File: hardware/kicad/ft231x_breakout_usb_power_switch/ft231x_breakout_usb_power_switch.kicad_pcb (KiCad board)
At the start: 2 copper layers, 60 x 31.2 mm, 50 parts, among them J1 USB_B_Micro_ALT, J2 USB_A_ALT, J3 Conn_01x08, J4 Conn_01x06, J5 Conn_01x08, Q3 2N7002, U1 SOT-23-6, U2 FT231XS, U3 SOT-23-6, U4 SOT-23-5

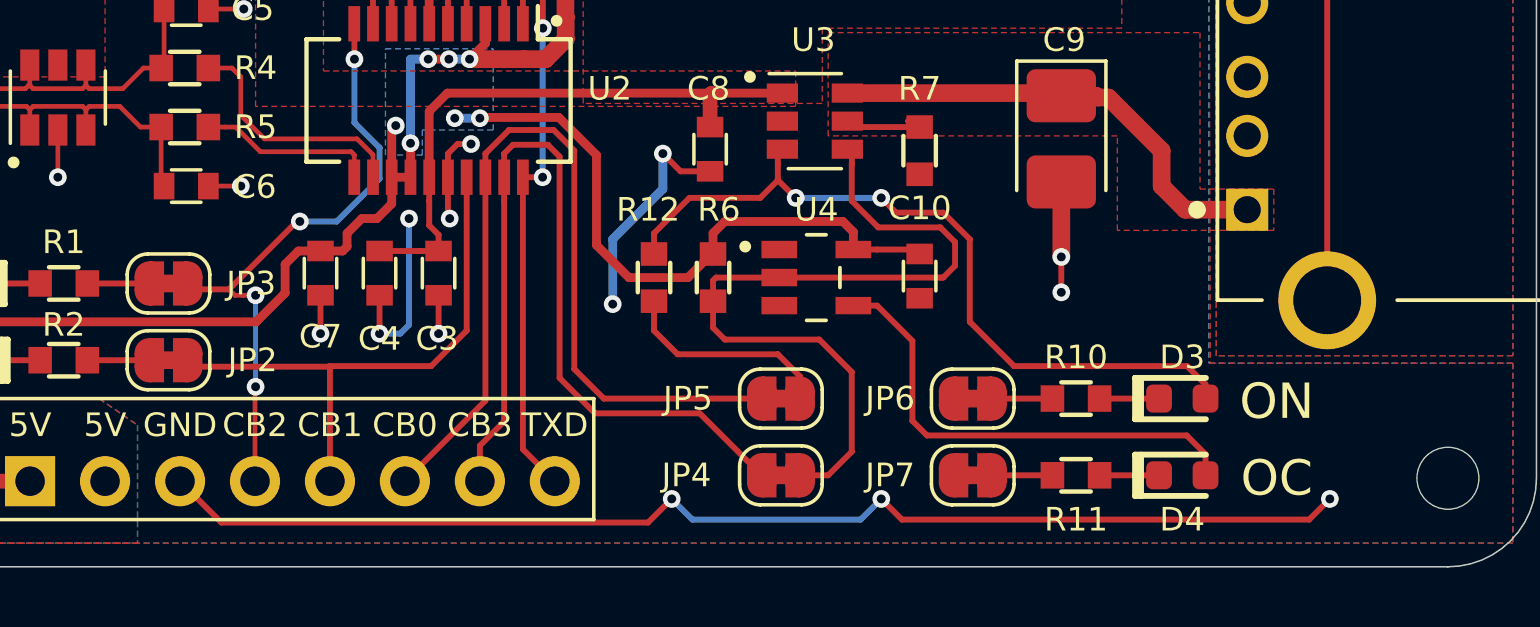
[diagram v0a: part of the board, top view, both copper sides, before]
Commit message: reset switch initial
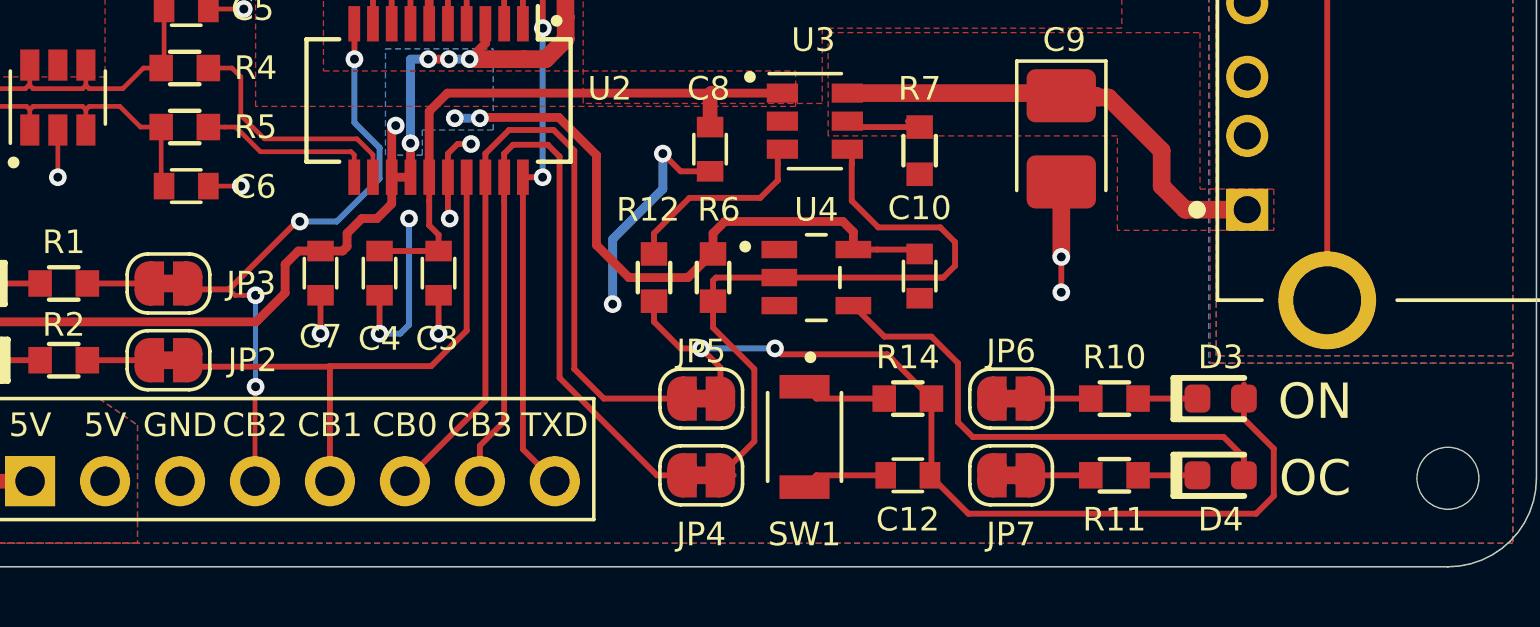
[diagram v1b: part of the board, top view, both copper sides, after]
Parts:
- added C12: 0.1uF, -Passive:C_0603, F.Cu at (148.7, 97.5)
- added R14: 1k, -Passive:R_0603, F.Cu at (148.7, 94.9)
- added SW1: SW_MEC_5G, -Switch:B3U-1000P, F.Cu at (145.2, 96.2)
- U1: value SOT-23-6 -> SRV05-4
- U3: value SOT-23-6 -> TPS2553DBVR
- U4: value SOT-23-5 -> SN74LVC1G04DBVR
- moved JP4 2.70 mm to (141.7, 97.5)
- moved JP5 2.70 mm to (141.7, 94.9)
- moved D3 1.30 mm to (159.3, 94.9)
- moved D4 1.30 mm to (159.3, 97.5)
- moved JP6 1.30 mm to (152.2, 94.9)
- moved JP7 1.30 mm to (152.2, 97.5)
- moved R10 1.30 mm to (155.7, 94.9)
- moved R11 1.30 mm to (155.7, 97.5)
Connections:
- JP5 pad 1: Net-(JP5-Pad1) -> /ENLED
- R12 pad 1: Net-(JP5-Pad1) -> /ENLED
- R12 pad 2: /ENLED -> Net-(R12-Pad2)
- U3 pad 3: /ENLED -> Net-(R12-Pad2)
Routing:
- net GND: track 111.3 -> 73.2 mm, vias 27 -> 24
- net Net-(JP5-Pad1): track 7.44 -> 0.00 mm
- net Net-(R12-Pad2): track 0.00 -> 6.60 mm
- net /ENLED: track 26.1 -> 32.5 mm
- net /FAULT: track 26.7 -> 23.6 mm
- net Net-(R14-Pad1): track 0.00 -> 2.87 mm
- net /GPO: track 30.0 -> 27.3 mm
- net /GPI: track 29.3 -> 26.6 mm
- net Net-(D4-Pad2): track 16.8 -> 17.6 mm

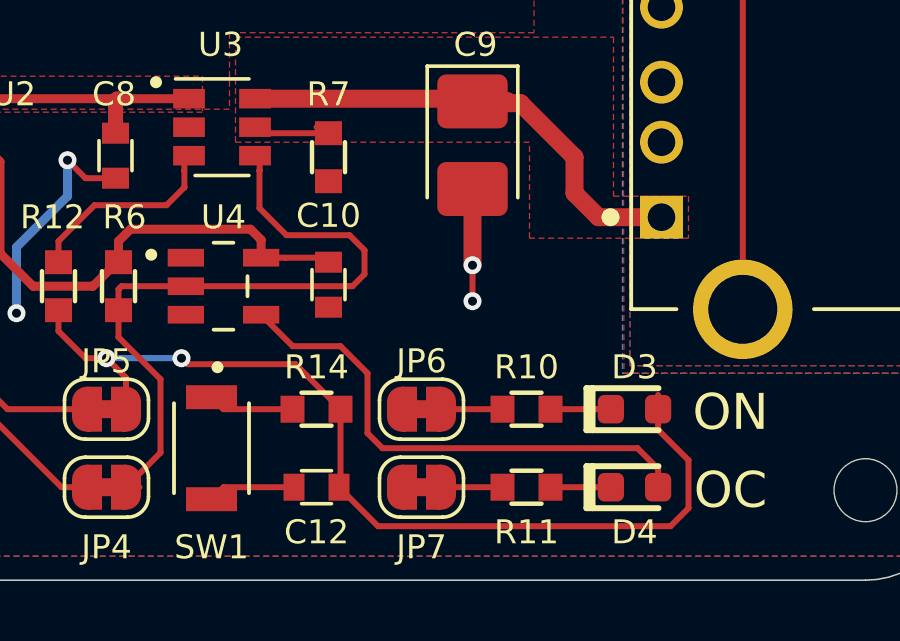
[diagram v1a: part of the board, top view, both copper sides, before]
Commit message: fix unconnected ground
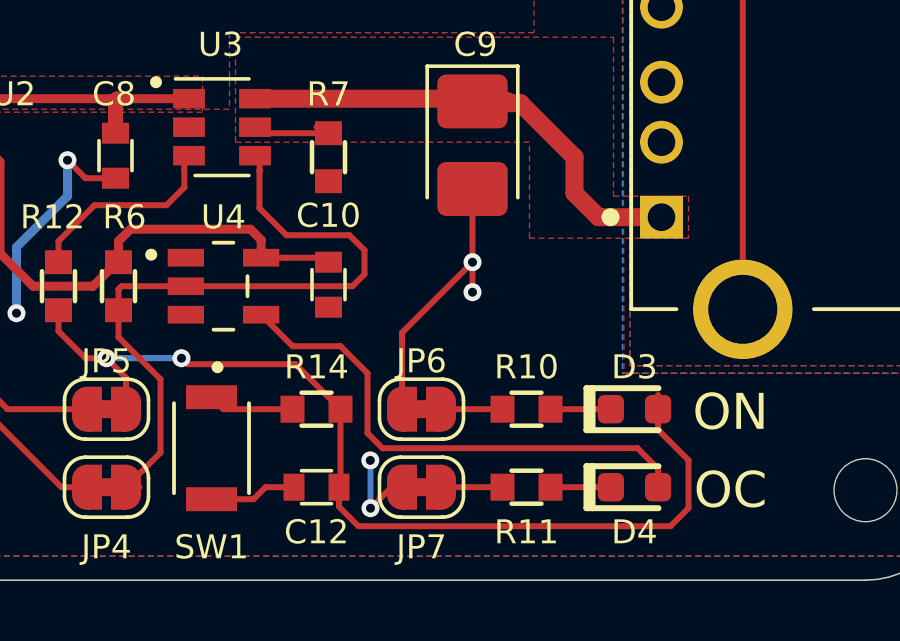
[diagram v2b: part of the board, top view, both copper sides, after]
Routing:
- net GND: track 73.2 -> 81.7 mm, vias 24 -> 26

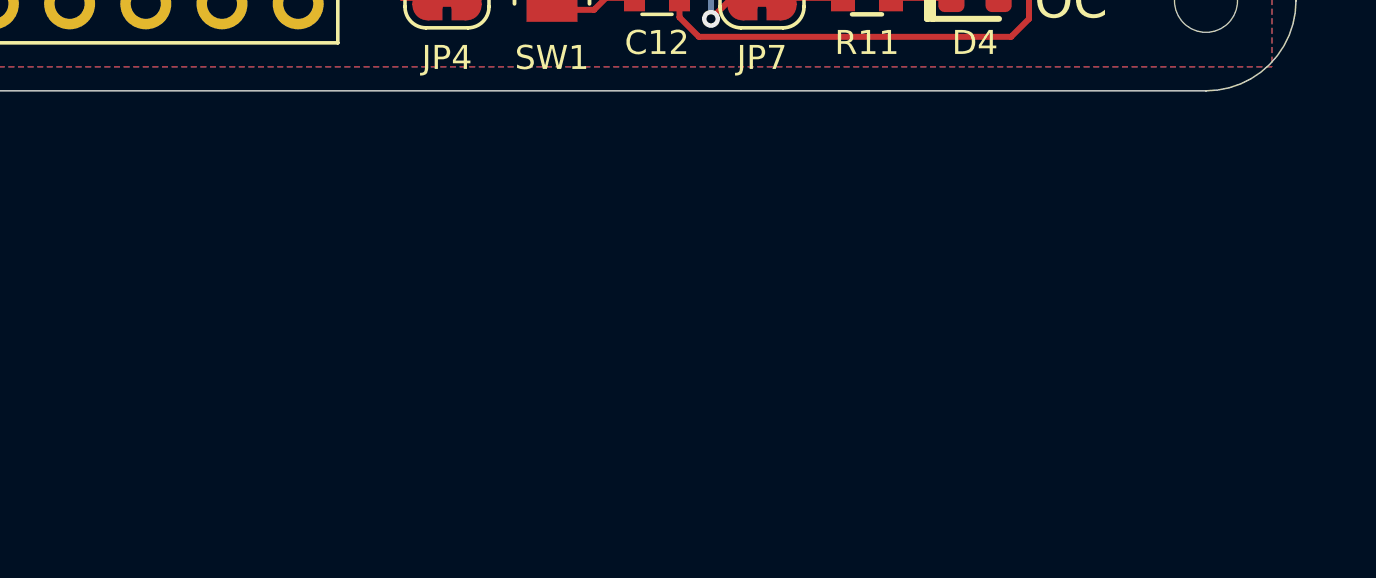
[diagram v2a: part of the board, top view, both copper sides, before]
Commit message: add optional pull down to enable
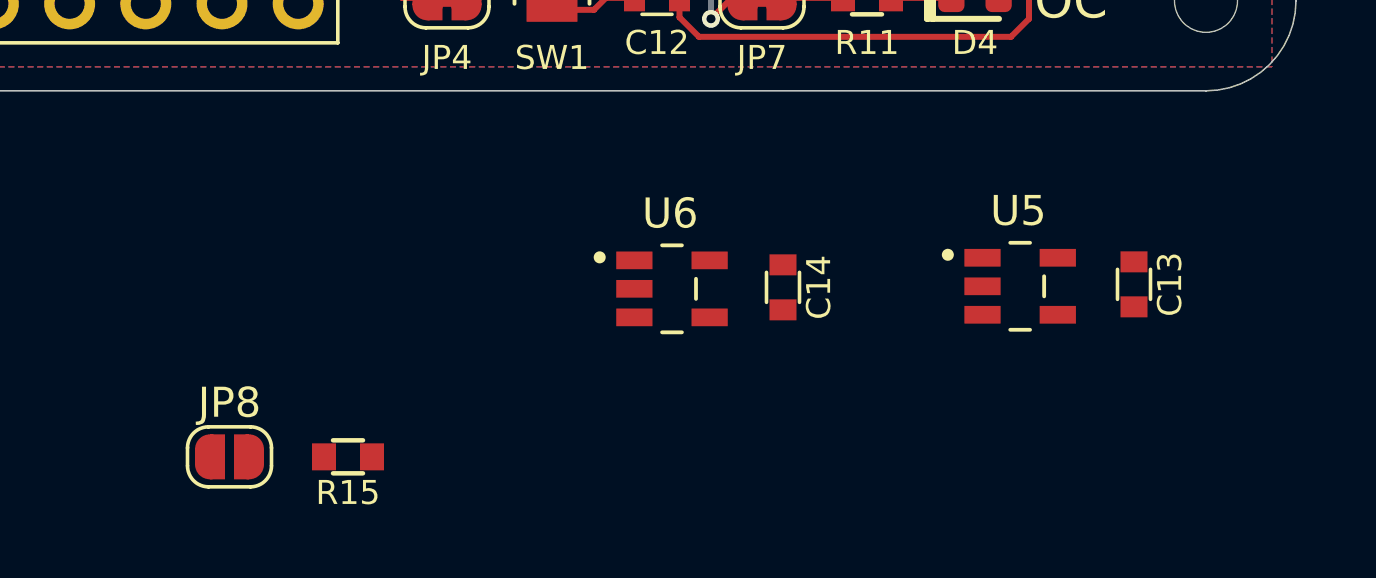
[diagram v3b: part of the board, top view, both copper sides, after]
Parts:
- added C13: 0.1uF, -Passive:C_0603, F.Cu at (164.6, 107.0)
- added C14: 0.1uF, -Passive:C_0603, F.Cu at (152.9, 107.2)
- added JP8: SolderJumper_2_Bridged_Alt, -Jumper:SolderJumper-2_P1.3mm_Un-Bridged_RoundedPad1.0x1.5mm, F.Cu at (134.4, 112.8)
- added R15: 1k, -Passive:R_0603, F.Cu at (138.4, 112.8)
- added U5: NC7SZ66M5X, -Chip:SOT-23-5, F.Cu at (160.8, 107.1)
- added U6: NC7SZ66M5X, -Chip:SOT-23-5, F.Cu at (149.2, 107.2)
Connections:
- net /ENLED renamed /EN
- C8 pad 1: +5V -> GND
- C8 pad 2: GND -> +5V
- J4 pad 4: /TXD -> /STXD
- J4 pad 6: /RESET -> /SRES
- Q3 pad 3: /RESET -> /RES
- R9 pad 1: /RESET -> /RES
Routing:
- net GND: track 81.7 -> 74.1 mm, vias 26 -> 24
- net +5V: track 21.8 -> 29.5 mm, vias 0 -> 2

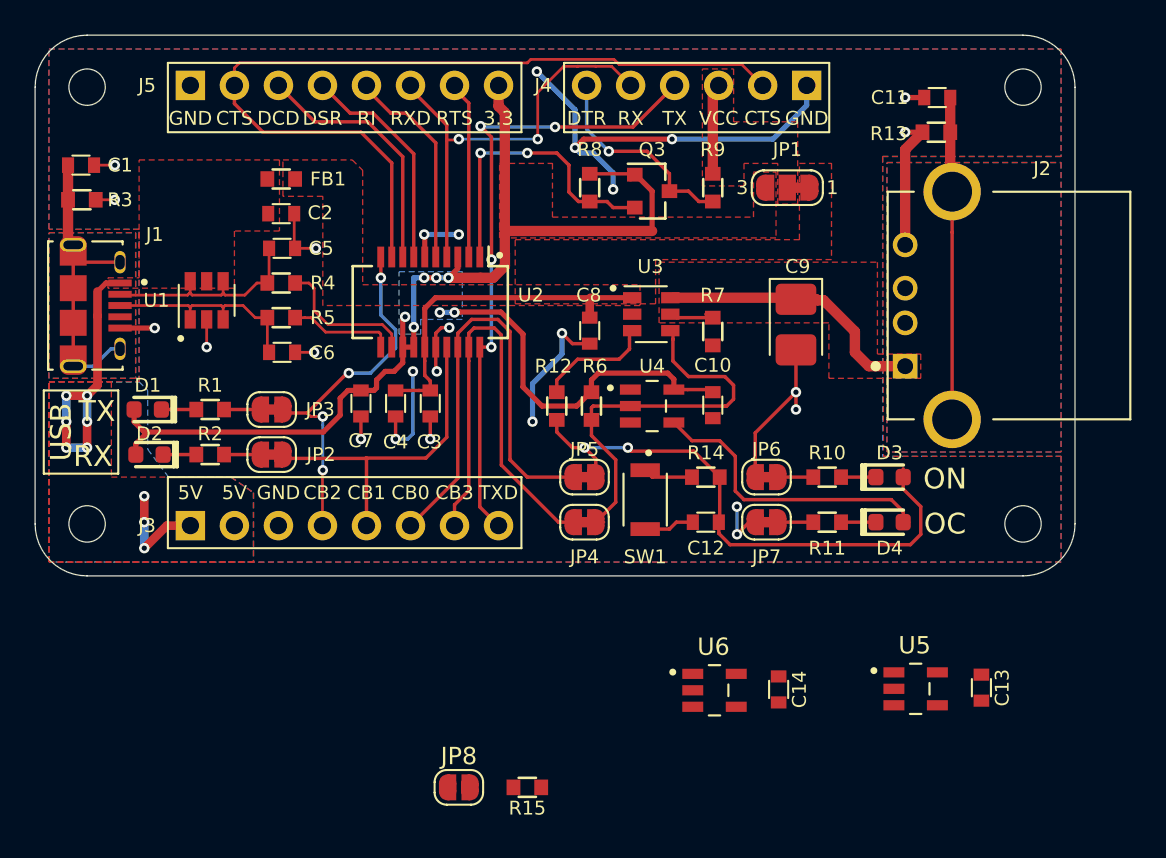
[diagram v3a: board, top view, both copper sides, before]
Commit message: Reset switch and bus switches routed
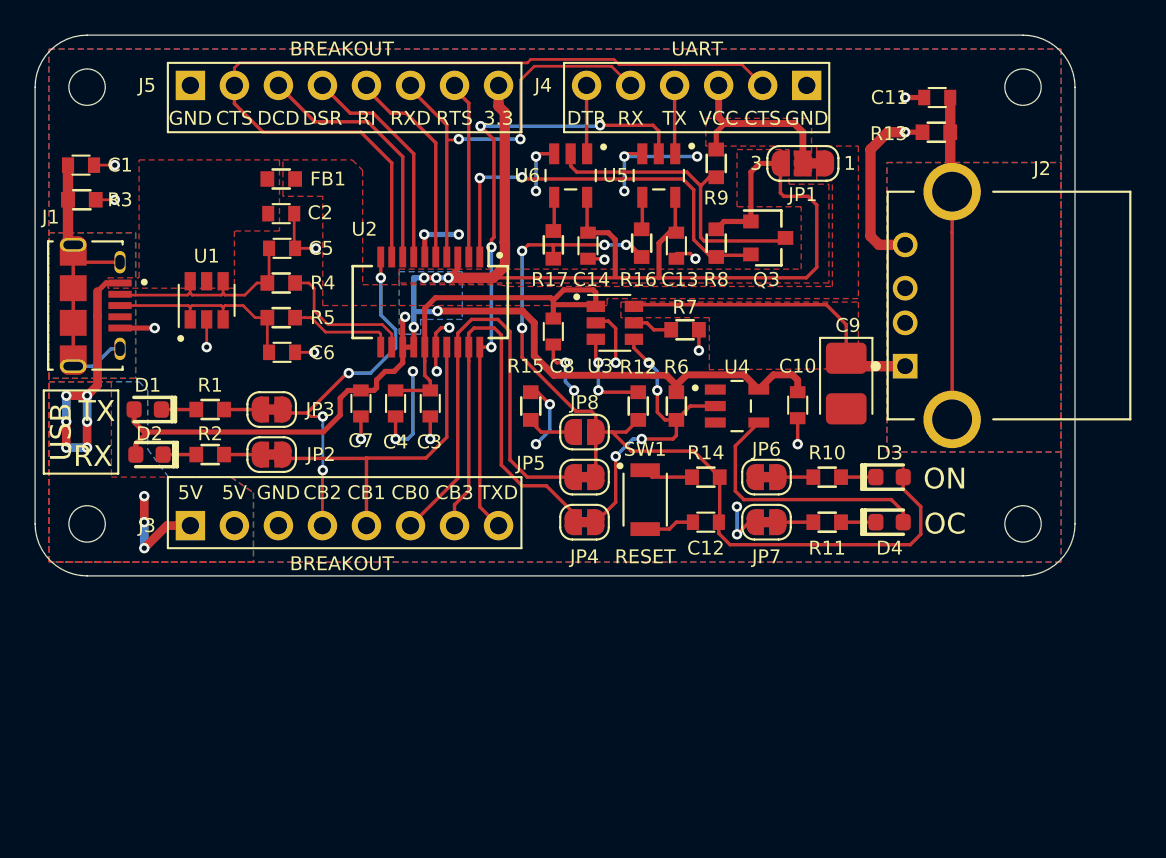
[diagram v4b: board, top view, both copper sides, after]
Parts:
- added R16: 1k, -Passive:R_0603, F.Cu at (145.0, 81.4)
- added R17: 1k, -Passive:R_0603, F.Cu at (139.9, 81.5)
- SW1: value SW_MEC_5G -> B3U-1000P
- moved U5 33.1 mm to (146.0, 77.5), turned to 270 degrees
- moved C13 31.0 mm to (147.0, 81.5)
- moved U6 30.8 mm to (140.9, 77.5), turned to 270 degrees
- moved C14 27.9 mm to (141.9, 81.5)
- moved R15 22.0 mm to (138.6, 90.8), turned to 270 degrees
- moved JP8 21.7 mm to (141.7, 92.3), turned to 180 degrees
- moved R8 7.97 mm to (149.3, 81.4)
- moved Q3 7.22 mm to (152.3, 81.1)
- moved C10 4.90 mm to (154.0, 90.8)
- moved R6 4.90 mm to (147.0, 90.8)
- moved U4 4.90 mm to (150.5, 90.8)
- moved R12 4.70 mm to (144.8, 90.8)
- moved C9 4.47 mm to (156.8, 89.5)
- moved U3 2.16 mm to (143.4, 86.0)
- moved C8 2.10 mm to (139.9, 86.5), turned to 90 degrees
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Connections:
- U5 pad 1: /TXD -> /STXD
- U5 pad 2: /STXD -> /TXD
- U5 pad 4: /EN -> Net-(R16-Pad2)
- U6 pad 1: /RES -> /SRES
- U6 pad 2: /SRES -> /RES
- U6 pad 4: /EN -> Net-(R17-Pad2)
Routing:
- net +3V3: track 82.5 -> 117.7 mm, vias 7 -> 6
- net /EN: track 32.9 -> 53.1 mm, vias 2 -> 4
- net /RES: track 0.00 -> 18.2 mm
- net /RESET: track 12.1 -> 0.00 mm, vias 1 -> 0
- net +5V: track 29.5 -> 21.6 mm, vias 2 -> 0
- net /DTR: track 17.2 -> 23.3 mm
- net /VOUT: track 5.30 -> 11.3 mm
- net /FAULT: track 23.6 -> 18.1 mm, vias 0 -> 4
- net GND: track 74.1 -> 69.2 mm, vias 24 -> 32
- net /STXD: track 0.00 -> 4.06 mm
- net /SRES: track 0.00 -> 4.04 mm
- net Net-(JP8-Pad2): track 0.00 -> 2.84 mm
- net Net-(R17-Pad2): track 0.00 -> 2.11 mm
- net Net-(C9-Pad1): track 16.8 -> 18.8 mm
- net Net-(R16-Pad2): track 0.00 -> 1.91 mm
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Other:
- board text added: "BREAKOUT"
- board text added: "RESET"
- board text added: "UART"

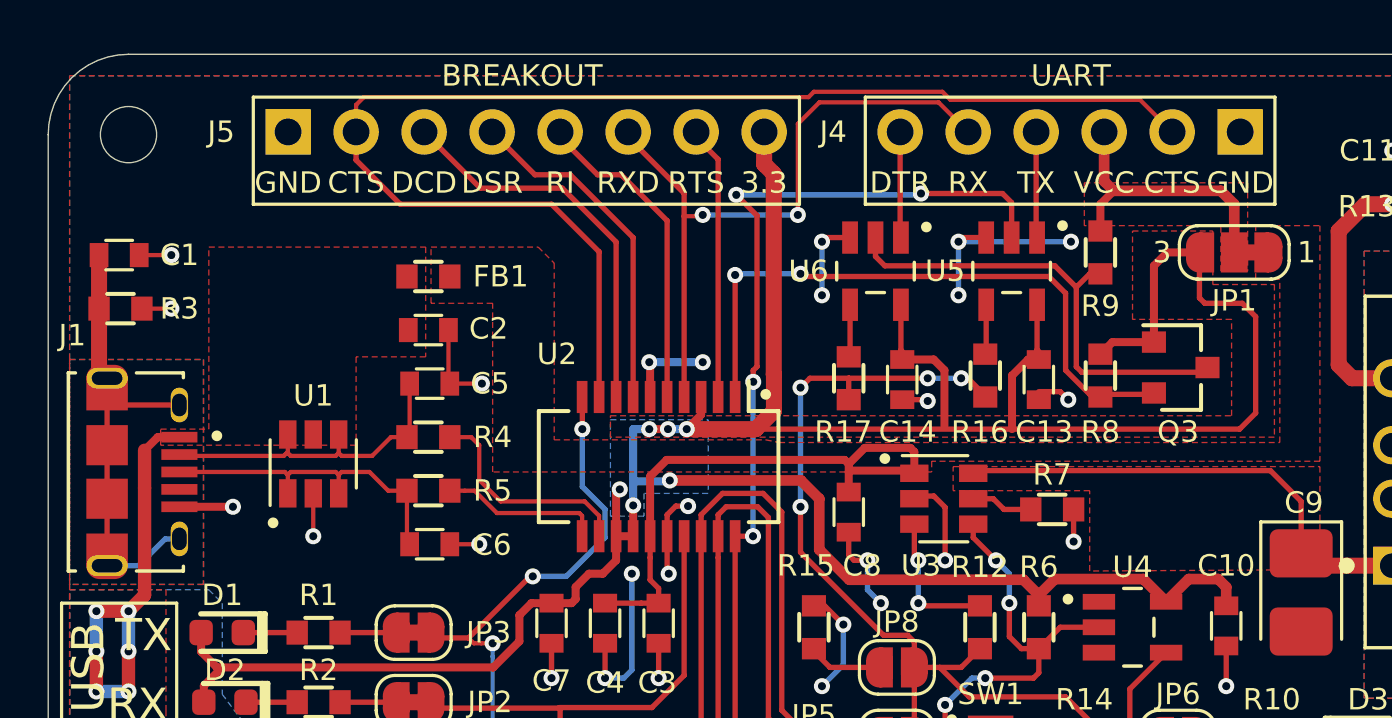
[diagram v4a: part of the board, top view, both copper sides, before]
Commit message: increase pad sizes for easier hand assembly
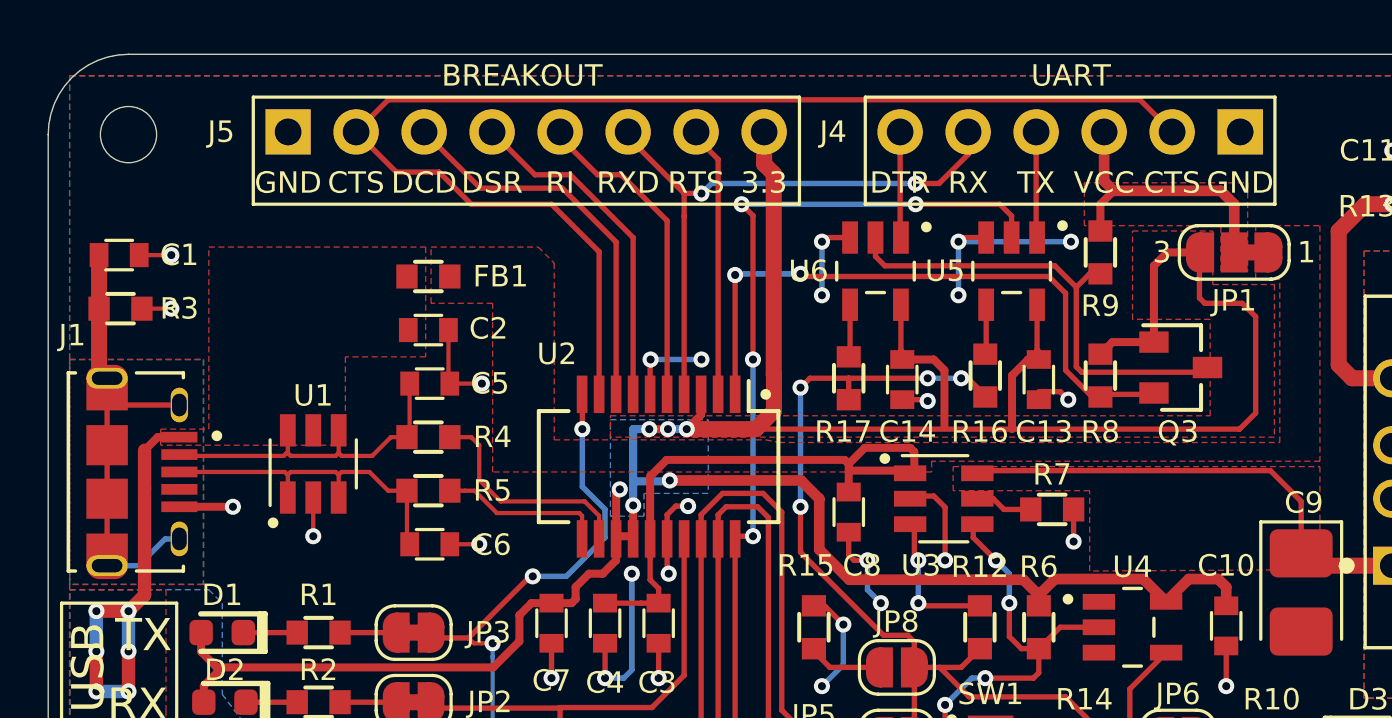
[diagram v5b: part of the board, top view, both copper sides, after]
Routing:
- net /RXD: track 25.4 -> 22.6 mm
- net /CTS: track 49.4 -> 47.9 mm
- net /TXD: track 36.0 -> 35.1 mm
